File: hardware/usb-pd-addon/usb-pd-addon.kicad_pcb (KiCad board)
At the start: 2 copper layers, 48 x 40 mm, 13 parts, among them J1 Conn_02x10_Odd_Even, J2 Conn_02x10_Odd_Even, J3 USB_TYPE_C, U1 FUSB302B, U2 AP2171W, U3 SN74AVC1T45DBVR, U4 SN74AVC1T45DBVR, U5 SN74AVC1T45DBVR, U6 SN74AVC1T45DBVR

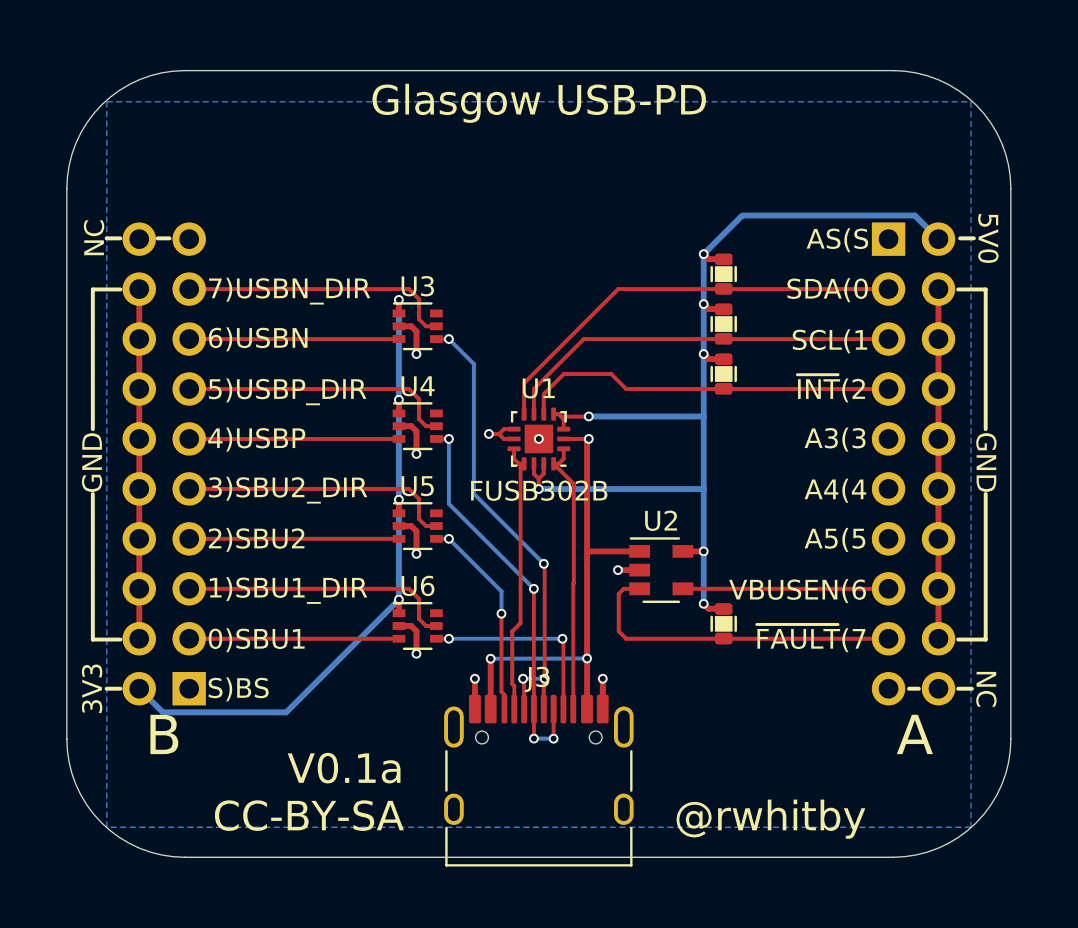
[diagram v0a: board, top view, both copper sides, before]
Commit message: v0.2a: Added adjustable LDOs for the level shifter reference voltages for USB and SBU pairs.
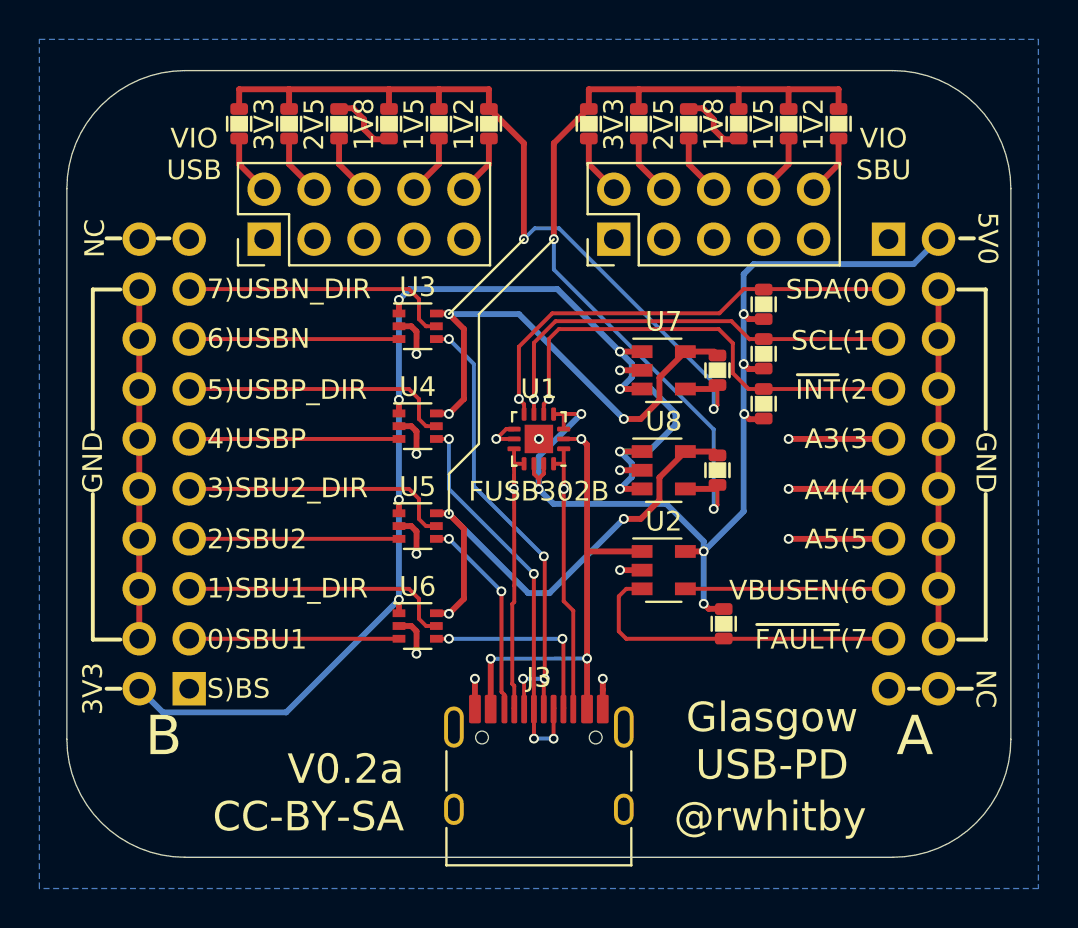
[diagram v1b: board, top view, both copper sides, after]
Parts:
- added J4: Conn_02x05_Odd_Even, Connector_PinHeader_2.54mm:PinHeader_2x05_P2.54mm_Vertical, F.Cu at (41.9, 40.6)
- added J5: Conn_02x05_Odd_Even, Connector_PinHeader_2.54mm:PinHeader_2x05_P2.54mm_Vertical, F.Cu at (59.7, 40.6)
- added R10: 4.7k, pkl_dipol:R_0603, F.Cu at (61.0, 34.8)
- added R11: 1.2k, pkl_dipol:R_0603, F.Cu at (48.3, 34.8)
- added R12: 6.8k, pkl_dipol:R_0603, F.Cu at (45.7, 34.8)
- added R13: 1.2k, pkl_dipol:R_0603, F.Cu at (66.0, 34.8)
- added R14: 6.8k, pkl_dipol:R_0603, F.Cu at (63.5, 34.8)
- added R15: 12k, pkl_dipol:R_0603, F.Cu at (50.8, 34.8)
- added R16: 12k, pkl_dipol:R_0603, F.Cu at (68.6, 34.8)
- added R17: 20k, pkl_dipol:R_0603, F.Cu at (53.3, 34.8)
- added R18: 20k, pkl_dipol:R_0603, F.Cu at (71.1, 34.8)
- added R5: 10k, pkl_dipol:R_0603, F.Cu at (65.0, 47.3)
- added R6: 10k, pkl_dipol:R_0603, F.Cu at (65.0, 52.4)
- added R7: 3.3k, pkl_dipol:R_0603, F.Cu at (40.6, 34.8)
- added R8: 3.3k, pkl_dipol:R_0603, F.Cu at (58.4, 34.8)
- added R9: 4.7k, pkl_dipol:R_0603, F.Cu at (43.2, 34.8)
- added U7: AP2127K-ADJ, Package_TO_SOT_SMD:SOT-23-5, F.Cu at (62.2, 47.3)
- added U8: AP2127K-ADJ, Package_TO_SOT_SMD:SOT-23-5, F.Cu at (62.2, 52.4)
- moved R1 2.55 mm to (67.3, 44.0), turned to 270 degrees
- moved R2 2.53 mm to (67.3, 46.5), turned to 270 degrees
- moved R3 2.53 mm to (67.3, 49.0), turned to 270 degrees
- moved U2 0.13 mm to (62.2, 57.5)
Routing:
- net Net-(R10-Pad1): track 0.00 -> 45.0 mm, vias 0 -> 2
- net Net-(R11-Pad1): track 0.00 -> 42.3 mm, vias 0 -> 2
- net +3V3: track 34.1 -> 63.5 mm, vias 4 -> 8
- net /VIO_SBU: track 0.00 -> 26.1 mm, vias 0 -> 3
- net /VIO_USB: track 0.00 -> 25.0 mm, vias 0 -> 3
- net Net-(J2-Pad9): track 0.00 -> 5.08 mm, vias 0 -> 1
- net Net-(J2-Pad13): track 0.00 -> 5.08 mm, vias 0 -> 1
- net Net-(J2-Pad11): track 0.00 -> 5.08 mm, vias 0 -> 1
- net /INT_N: track 19.2 -> 23.6 mm, vias 0 -> 1
- net Net-(R13-Pad2): track 0.00 -> 3.49 mm
- net Net-(R11-Pad2): track 0.00 -> 3.49 mm
- net /1V2_SBU: track 0.00 -> 3.07 mm
- net /2V5_USB: track 0.00 -> 3.07 mm
- net /1V8_USB: track 0.00 -> 3.07 mm
- net /1V2_USB: track 0.00 -> 3.07 mm
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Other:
- board text added: "1V2"
- board text added: "1V5"
- board text added: "1V8"
- board text added: "2V5"
- board text added: "V0.2a CC-BY-SA"
- board text added: "VIO SBU"
- board text added: "VIO USB"
- board text removed: "AS(S"
- board text removed: "S)AS"
- board text removed: "V0.1a CC-BY-SA"

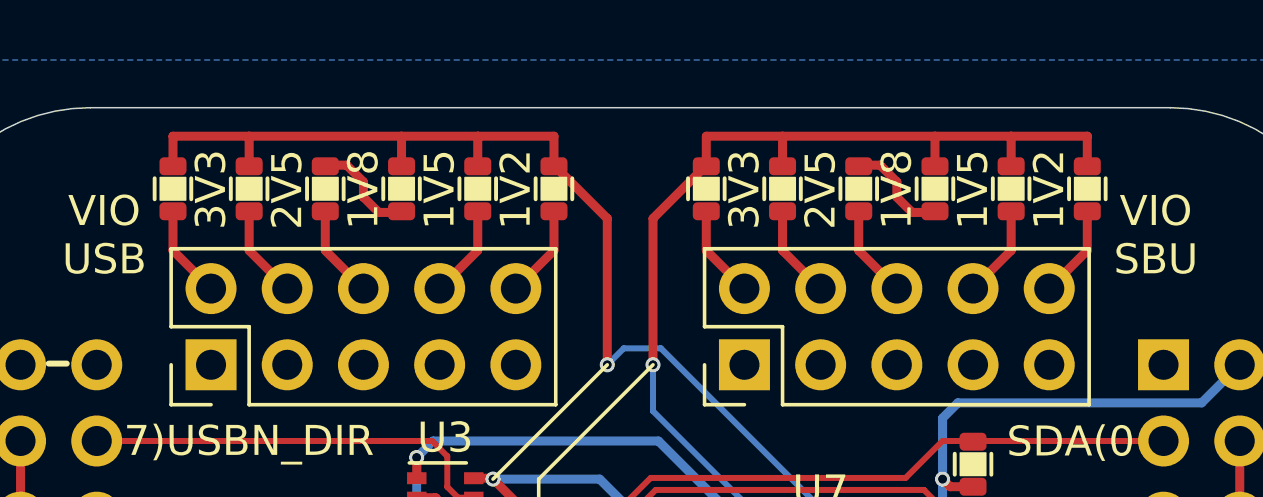
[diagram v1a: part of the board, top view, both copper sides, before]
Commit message: Updated USB-C symbol, no functional change.
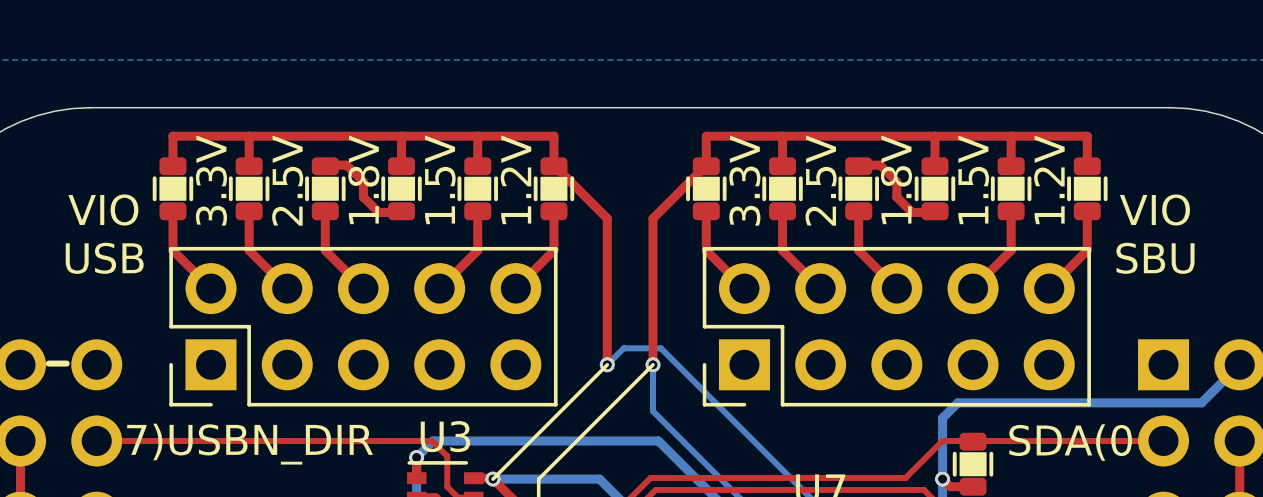
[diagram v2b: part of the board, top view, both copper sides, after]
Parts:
- R1, R2, R3: value 1K -> 2K2
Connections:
- J3 pad S1: (no net) -> GND
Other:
- board text added: "1.2V"
- board text added: "1.5V"
- board text added: "1.8V"
- board text added: "2.5V"
- board text added: "3.3V"
- board text removed: "1V2"
- board text removed: "1V5"
- board text removed: "1V8"
- board text removed: "2V5"

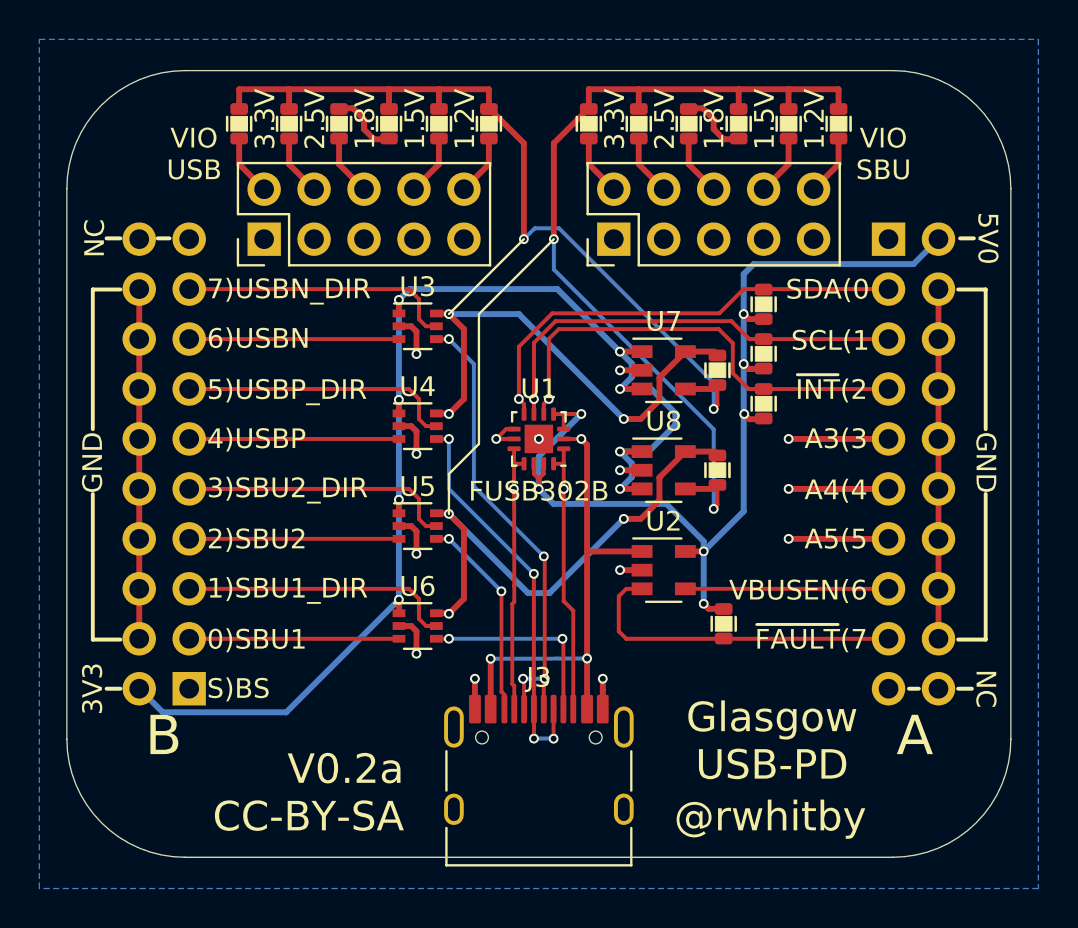
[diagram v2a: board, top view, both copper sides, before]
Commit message: Added more resistors to fine tune level shifter reference voltages.
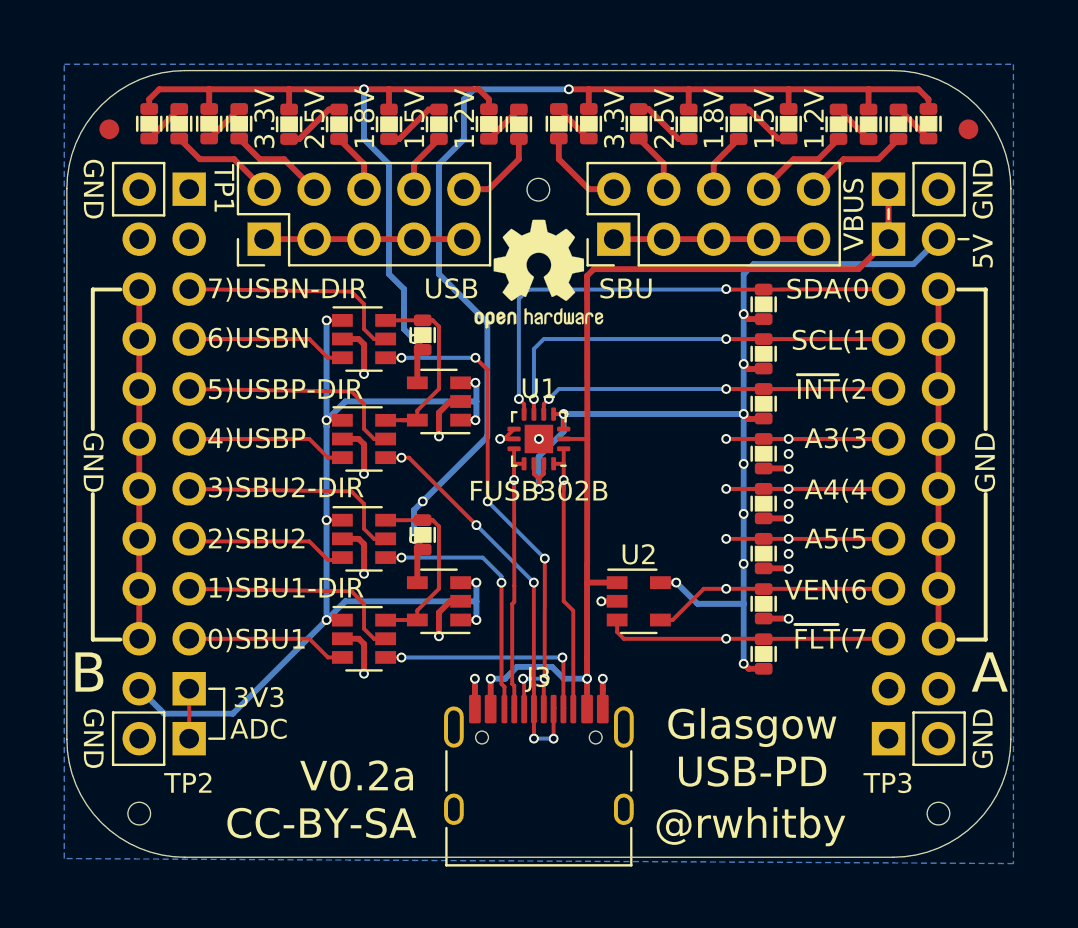
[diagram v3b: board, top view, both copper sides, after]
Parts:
- removed the R18 at (71.1, 34.8)
- removed the R8 at (58.4, 34.8)
- added FID1: Fiducial, Fiducial:Fiducial_1mm_Mask2mm, F.Cu at (34.0, 35.1)
- added FID2: Fiducial, Fiducial:Fiducial_1mm_Mask2mm, F.Cu at (77.7, 35.1)
- added J6: EXT, Connector_PinHeader_2.54mm:PinHeader_1x02_P2.54mm_Vertical, F.Cu at (73.7, 38.1)
- added J7: TP1, Connector_PinHeader_2.54mm:PinHeader_1x02_P2.54mm_Vertical, F.Cu at (38.1, 38.1)
- added J8: TP2, Connector_PinHeader_2.54mm:PinHeader_1x02_P2.54mm_Vertical, F.Cu at (38.1, 66.0)
- added J9: TP3, Connector_PinHeader_2.54mm:PinHeader_1x02_P2.54mm_Vertical, F.Cu at (73.7, 66.0)
- added LOGO1: Logo_Open_Hardware_Small, Symbol:OSHW-Logo2_7.3x6mm_SilkScreen, F.Cu at (55.9, 42.4)
- added LOGO2: Logo_Open_Hardware_Small, Symbol:OSHW-Logo2_7.3x6mm_SilkScreen, B.Cu at (55.9, 42.4)
- added R10: 10k, pkl_dipol:R_0603, F.Cu at (50.0, 55.7)
- added R11: 1K2, pkl_dipol:R_0603, F.Cu at (36.1, 34.8)
- added R13: 0R, pkl_dipol:R_0603, F.Cu at (39.1, 34.8)
- added R17: 1K5, pkl_dipol:R_0603, F.Cu at (48.3, 34.8)
- added R19: 0R, pkl_dipol:R_0603, F.Cu at (53.3, 34.8)
- added R21: 2K0, pkl_dipol:R_0603, F.Cu at (56.9, 34.8)
- added R22: 1K2, pkl_dipol:R_0603, F.Cu at (58.4, 34.8)
- added R24: 0R, pkl_dipol:R_0603, F.Cu at (63.5, 34.8)
- added R28: 1K5, pkl_dipol:R_0603, F.Cu at (72.6, 34.8)
- added R29: 20K, pkl_dipol:R_0603, F.Cu at (74.2, 34.8)
- added R30: 0R, pkl_dipol:R_0603, F.Cu at (75.7, 34.8)
- added R4: 2K2, pkl_dipol:R_0603, F.Cu at (67.3, 51.5)
- added R7: 1K, pkl_dipol:R_0603, F.Cu at (67.3, 59.2)
- added R9: 10k, pkl_dipol:R_0603, F.Cu at (50.0, 45.5)
- added TH1: Mounting_Hole, pkl_pads:ToolingHole, F.Cu at (33.6, 67.8)
- added TH2: Mounting_Hole, pkl_pads:ToolingHole, F.Cu at (74.2, 67.8)
- added TH3: Mounting_Hole, pkl_pads:ToolingHole, F.Cu at (53.9, 36.1)
- R12: renamed from R7; value 3.3k -> 2K0
- R14: renamed from R9; value 4.7k -> 4K7
- R15: renamed from R11; value 1.2k -> 1K2
- R16: renamed from R12; value 6.8k -> 6K8
- R18: renamed from R15; value 12k -> 10K
- R20: renamed from R17; value 20k -> 20K
- R23: renamed from R10; value 4.7k -> 4K7
- R25: renamed from R14; value 6.8k -> 6K8
- R26: renamed from R13; value 1.2k -> 1K2
- R27: renamed from R16; value 12k -> 10K
- R5, R6: value 10k -> 2K2
- U3, U4, U5, U6: footprint Package_TO_SOT_SMD:SOT-363_SC-70-6 -> Package_TO_SOT_SMD:SOT-23-6
- moved U8 13.2 mm to (50.8, 59.1), turned to 180 degrees
- moved U7 11.5 mm to (50.8, 48.9), turned to 180 degrees
- moved R5 7.18 mm to (67.3, 54.1), turned to 90 degrees
- moved U4 6.35 mm to (47.0, 55.9)
- moved U5 5.20 mm to (47.0, 50.8)
- moved R15 5.08 mm to (43.2, 34.8), turned to 90 degrees
- moved R6 4.85 mm to (67.3, 56.6), turned to 90 degrees
- moved R12 3.05 mm to (37.6, 34.8)
- moved U3 2.80 mm to (47.0, 45.7)
- moved U6 2.80 mm to (47.0, 61.0)
- moved R8 2.55 mm to (67.3, 61.7), turned to 270 degrees
- moved R25 2.54 mm to (66.0, 34.8), turned to 90 degrees
- moved R27 2.54 mm to (71.1, 34.8), turned to 90 degrees
- moved R14 2.54 mm to (40.6, 34.8), turned to 90 degrees
- moved R26 2.54 mm to (68.6, 34.8), turned to 90 degrees
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- renumbered R4 to R8
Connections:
- net /FAULT_N renamed /FLT_N
- net /VBUS_EN renamed /VEN
- J2 pad 1: /AS -> /VBUS
- J2 pad 11: Net-(J2-Pad11) -> /A4
- J2 pad 13: Net-(J2-Pad13) -> /A5
- J2 pad 9: Net-(J2-Pad9) -> /A3
- R1 pad 1: /SDA -> +5V
- R1 pad 2: +5V -> /SDA
- R14 pad 1: Net-(R11-Pad1) -> /2V5_USB
- R14 pad 2: /2V5_USB -> Net-(R13-Pad1)
- R15 pad 1: Net-(R11-Pad1) -> Net-(R15-Pad1)
- R15 pad 2: Net-(R11-Pad2) -> /ADJ_USB
- R16 pad 1: Net-(R11-Pad2) -> /1V8_USB
- R16 pad 2: /1V8_USB -> Net-(R15-Pad1)
- R18 pad 1: Net-(R11-Pad1) -> /1V5_USB
- R18 pad 2: /1V5_USB -> Net-(R17-Pad1)
- R2 pad 1: /SCL -> +5V
- R2 pad 2: +5V -> /SCL
- R20 pad 1: Net-(R11-Pad1) -> /1V2_USB
- R20 pad 2: /1V2_USB -> Net-(R19-Pad1)
- R23 pad 1: Net-(R10-Pad1) -> /2V5_SBU
- R23 pad 2: /2V5_SBU -> Net-(R23-Pad2)
- R25 pad 1: Net-(R13-Pad2) -> /1V8_SBU
- R25 pad 2: /1V8_SBU -> Net-(R25-Pad2)
- R26 pad 1: Net-(R10-Pad1) -> Net-(R25-Pad2)
- R26 pad 2: Net-(R13-Pad2) -> /ADJ_SBU
- R27 pad 1: Net-(R10-Pad1) -> /1V5_SBU
- R27 pad 2: /1V5_SBU -> Net-(R27-Pad2)
- R3 pad 1: /INT_N -> +5V
- R3 pad 2: +5V -> /INT_N
- R5 pad 1: /VIO_USB -> Net-(R5-Pad1)
- R5 pad 2: Net-(R11-Pad1) -> /A4
- R6 pad 1: /VIO_SBU -> Net-(R6-Pad1)
- R6 pad 2: Net-(R10-Pad1) -> /A5
- U4 pad 3: /USBP_3V3 -> /SBU2_3V3
- U4 pad 4: /USBP -> /SBU2
- U4 pad 5: /USBP_DIR -> /SBU2_DIR
- U4 pad 6: /VIO_USB -> /VIO_SBU
- U5 pad 3: /SBU2_3V3 -> /USBP_3V3
- U5 pad 4: /SBU2 -> /USBP
- U5 pad 5: /SBU2_DIR -> /USBP_DIR
- U5 pad 6: /VIO_SBU -> /VIO_USB
- U7 pad 4: Net-(R11-Pad1) -> /ADJ_USB
- U8 pad 4: Net-(R10-Pad1) -> /ADJ_SBU
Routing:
- net /ADJ_SBU: track 0.00 -> 56.6 mm, vias 0 -> 3
- net Net-(R10-Pad1): track 45.0 -> 0.00 mm, vias 2 -> 0
- net Net-(R11-Pad1): track 42.3 -> 2.15 mm, vias 2 -> 0
- net /ADJ_USB: track 0.00 -> 38.0 mm, vias 0 -> 2
- net GND: track 52.6 -> 78.6 mm, vias 11 -> 15
- net /VBUS: track 24.8 -> 50.4 mm, vias 3 -> 2
- net /VIO_SBU: track 26.1 -> 10.5 mm, vias 3 -> 0
- net /VIO_USB: track 25.0 -> 10.5 mm, vias 3 -> 0
- net +3V3: track 63.5 -> 53.9 mm
- net /A5: track 0.00 -> 8.25 mm, vias 0 -> 2
- net /A4: track 0.00 -> 8.25 mm, vias 0 -> 2
- net /A3: track 0.00 -> 8.25 mm, vias 0 -> 2
- net /INT_N: track 23.6 -> 18.4 mm, vias 1 -> 2
- net Net-(J2-Pad9): track 5.08 -> 0.00 mm, vias 1 -> 0
- net Net-(J2-Pad13): track 5.08 -> 0.00 mm, vias 1 -> 0
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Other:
- board text added: "1)SBU1-DIR"
- board text added: "3)SBU2-DIR"
- board text added: "3V3 ADC"
- board text added: "5)USBP-DIR"
- board text added: "5V"
- board text added: "6)VEN"
- board text added: "7)USBN-DIR"
- board text added: "7)~FLT"
- board text added: "JLCJLCJLCJLC"
- board text added: "SBU"
- board text added: "SBU1-DIR(1"
- board text added: "SBU2-DIR(3"
- board text added: "TP1"
- board text added: "TP2"
- board text added: "TP3"
- board text added: "USB"
- board text added: "USBN-DIR(7"
- board text added: "USBP-DIR(5"
- board text added: "VBUS"
- board text added: "VEN(6"
- board text added: "~FLT~(7"
- board text removed: "1)SBU1_DIR"
- board text removed: "3)SBU2_DIR"
- board text removed: "3V3"
- board text removed: "5)USBP_DIR"
- board text removed: "5V0"
- board text removed: "6)VBUSEN"
- board text removed: "7)USBN_DIR"
- board text removed: "7)~FAULT"
- board text removed: "BS(S"
- board text removed: "NC"
- board text removed: "S)BS"
- board text removed: "SBU1_DIR(1"
- board text removed: "SBU2_DIR(3"
- board text removed: "USBN_DIR(7"
- board text removed: "USBP_DIR(5"
- board text removed: "VBUSEN(6"
- board text removed: "VIO SBU"
- board text removed: "VIO USB"
- board text removed: "~FAULT~(7"
